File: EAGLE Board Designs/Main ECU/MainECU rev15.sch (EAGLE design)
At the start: 334 parts, among them J1 CONNECTOR-24_CONNECTOR-24_, J2 CONNECTOR-24_CONNECTOR-24_, K1 RELAY_DPDT_07DSMT, K2 RELAY_DPDT_07DSMT, K3 RELAY_DPDT_07DSMT, K4 RELAY_DPDT_07DSMT, K5 RELAY_DPDT_07DSMT, Q1 TRANSISTOR_N_MOS__DMG3406L-7, Q2 TRANSISTOR_P_MOS_SOT-23_DMP30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, Q3 TRANSISTOR_P_MOS_SOT-23_DMP30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, Q4 TRANSISTOR_N_MOS__DMG3406L-7, T1 TRANSFORMER_HM2112ZNLT, U1 VOLTAGE_REGULATOR_SOT-223_3.3V, U10 LOGICGATE_OR, U11 LOGICGATE_OR, U12 LOGICGATE_OR, U13 LOGICGATE_NOR, U14 TCAN1051HQV-Q1, U15 LOGICGATE_AND_DCK3, U16 MAX3074EESA+, U17 LTC1563, U18 LTC1563, U19 LTC1563, U2 LTC6820, U20 LTC1563, U21 LTC1563, U22 LTC1563, U23 LTC1563, U24 OPAMP_2_CHANNEL_OPA_2991, U25 OPAMP_2_CHANNEL_OPA_2991, U26 OPAMP_2_CHANNEL_OPA_2991, U27 OPAMP_2_CHANNEL_OPA_2991, U28 LTC1563, U29 TCAN1051HQV-Q1, U3 LTC6820, U30 TCAN1051HQV-Q1, U31 ADM8316WBX30, U4 TCAN1051HQV-Q1, U5 LTC1563, U6 MCP3208, U7 OPAMP_1_CHANNEL_OPA991, U8 LOGICGATE_OR, U9 LOGICGATE_OR

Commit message: going crazy
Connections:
- net BRAKELIGHT_EN: now also A2.D8; no longer A2.D7
- net INVERTER_24V_EN: now also A2.D7; no longer A2.D8

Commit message: DRC
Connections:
- removed net !STEERING_2_CS: A2.(CS)D10
- new net LPA10: R77.2, R81.2, U18.LPA
- net BRAKELIGHT_EN: now also A2.D6; no longer A2.D8
- net LPA: no longer R77.2, R81.2, U18.LPA
- net SHDN_C_READ: now also A2.(CS)D10; no longer A2.A17
- net SOFTWARE_OK: now also A2.D8; no longer A2.D28

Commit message: shifted stuff over
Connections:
- net BRAKE_1_EXT: now also J2.18; no longer J2.17
- net BRAKE_2_EXT: now also J2.17; no longer J2.18
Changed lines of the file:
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@@
-</segment>
-</net>
-<net name="BRAKE_1_EXT" class="0">
-<segment>
-<wire x1="111.76" y1="127" x2="119.38" y2="127" width="0.1524" layer="91"/>
-<label x="119.38" y="127" size="1.27" layer="95" xref="yes"/>
-<pinref part="J2" gate="G$1" pin="17"/>
 </segment>
 </net>
 <net name="BRAKE_2_EXT" class="0">
 <segment>
-<wire x1="111.76" y1="124.46" x2="119.38" y2="124.46" width="0.1524" layer="91"/>
-<label x="119.38" y="124.46" size="1.27" layer="95" xref="yes"/>
-<pinref part="J2" gate="G$1" pin="18"/>
+<wire x1="111.76" y1="127" x2="119.38" y2="127" width="0.1524" layer="91"/>
+<pinref part="J2" gate="G$1" pin="17"/>
+<label x="119.38" y="127" size="1.27" layer="95" xref="yes"/>
 </segment>
 </net>
@@
 </segment>
 </net>
+<net name="BRAKE_1_EXT" class="0">
+<segment>
+<wire x1="111.76" y1="124.46" x2="119.38" y2="124.46" width="0.1524" layer="91"/>
+<label x="119.38" y="124.46" size="1.27" layer="95" xref="yes"/>
+<pinref part="J2" gate="G$1" pin="18"/>
+</segment>
+</net>

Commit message: finito
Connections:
- new net LPA20: R73.2, R75.2, U17.LPA
- net LPA: no longer R73.2, R75.2, U17.LPA

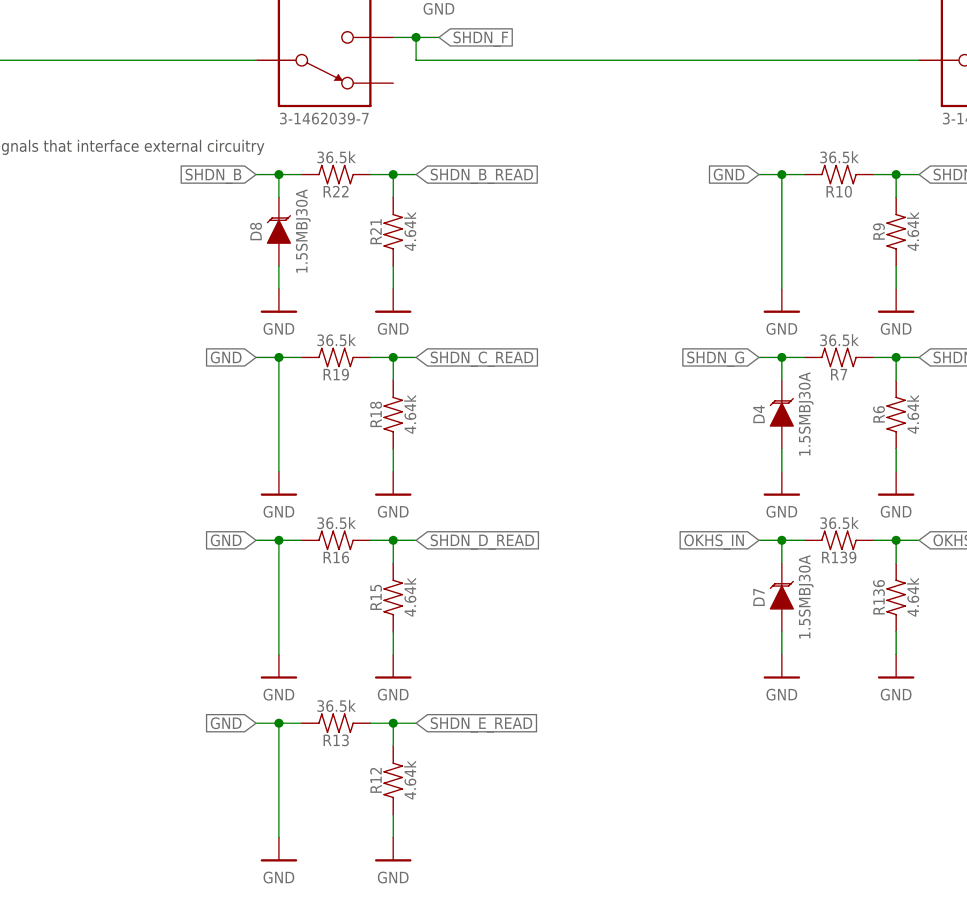
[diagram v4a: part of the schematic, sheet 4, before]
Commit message: mikhail prelim review
changes that need to be made have been recorded
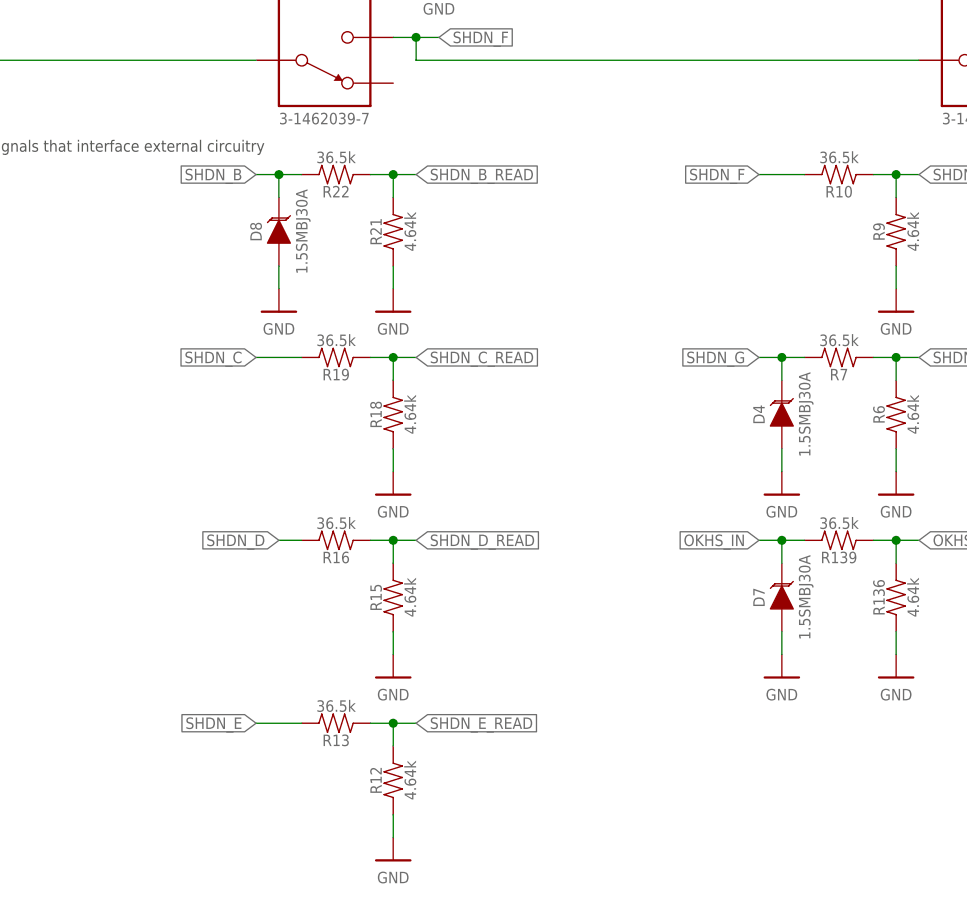
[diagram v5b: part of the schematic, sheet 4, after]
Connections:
- net GND: no longer R10.2, R13.2, R16.2, R19.2
- net SHDN_C: now also R19.2
- net SHDN_D: now also R16.2
- net SHDN_E: now also R13.2
- net SHDN_F: now also R10.2
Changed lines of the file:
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@@
 <part name="P289" library="HyTechSupplies" deviceset="GND" device=""/>
 <part name="R18" library="HyTechDevices" deviceset="RESISTOR_?_*" device="0603" technology="4.64K" value="RESISTOR_0603_4.64K"/>
-<part name="P290" library="HyTechSupplies" deviceset="GND" device=""/>
 <part name="R16" library="HyTechDevices" deviceset="RESISTOR_?_*" device="0603" technology="36.5K" value="RESISTOR_0603_36.5K"/>
 <part name="P291" library="HyTechSupplies" deviceset="GND" device=""/>
 <part name="R15" library="HyTechDevices" deviceset="RESISTOR_?_*" device="0603" technology="4.64K" value="RESISTOR_0603_4.64K"/>
-<part name="P292" library="HyTechSupplies" deviceset="GND" device=""/>
 <part name="R13" library="HyTechDevices" deviceset="RESISTOR_?_*" device="0603" technology="36.5K" value="RESISTOR_0603_36.5K"/>
 <part name="P293" library="HyTechSupplies" deviceset="GND" device=""/>
 <part name="R12" library="HyTechDevices" deviceset="RESISTOR_?_*" device="0603" technology="4.64K" value="RESISTOR_0603_4.64K"/>
-<part name="P294" library="HyTechSupplies" deviceset="GND" device=""/>
 <part name="R10" library="HyTechDevices" deviceset="RESISTOR_?_*" device="0603" technology="36.5K" value="RESISTOR_0603_36.5K"/>
 <part name="P295" library="HyTechSupplies" deviceset="GND" device=""/>
 <part name="R9" library="HyTechDevices" deviceset="RESISTOR_?_*" device="0603" technology="4.64K" value="RESISTOR_0603_4.64K"/>
-<part name="P296" library="HyTechSupplies" deviceset="GND" device=""/>
 <part name="R7" library="HyTechDevices" deviceset="RESISTOR_?_*" device="0603" technology="36.5K" value="RESISTOR_0603_36.5K"/>
 <part name="P297" library="HyTechSupplies" deviceset="GND" device=""/>
@@
 <attribute name="RESISTANCE" x="59.69" y="74.93" size="1.27" layer="96" rot="R90" align="top-center"/>
 </instance>
-<instance part="P290" gate="1" x="45.72" y="66.04" smashed="yes">
-<attribute name="VALUE" x="45.72" y="64.77" size="1.27" layer="96" align="top-center"/>
-</instance>
 <instance part="R16" gate="G$1" x="50.8" y="60.96" smashed="yes" rot="R180">
 <attribute name="NAME" x="52.07" y="59.69" size="1.27" layer="95" rot="R180" align="bottom-center"/>
@@
 <attribute name="RESISTANCE" x="59.69" y="54.61" size="1.27" layer="96" rot="R90" align="top-center"/>
 </instance>
-<instance part="P292" gate="1" x="45.72" y="45.72" smashed="yes">
-<attribute name="VALUE" x="45.72" y="44.45" size="1.27" layer="96" align="top-center"/>
-</instance>
 <instance part="R13" gate="G$1" x="50.8" y="40.64" smashed="yes" rot="R180">
 <attribute name="NAME" x="52.07" y="39.37" size="1.27" layer="95" rot="R180" align="bottom-center"/>
@@
 <attribute name="RESISTANCE" x="59.69" y="34.29" size="1.27" layer="96" rot="R90" align="top-center"/>
 </instance>
-<instance part="P294" gate="1" x="45.72" y="25.4" smashed="yes">
-<attribute name="VALUE" x="45.72" y="24.13" size="1.27" layer="96" align="top-center"/>
-</instance>
 <instance part="R10" gate="G$1" x="106.68" y="101.6" smashed="yes" rot="R180">
 <attribute name="NAME" x="107.95" y="100.33" size="1.27" layer="95" rot="R180" align="bottom-center"/>
@@
 <attribute name="RESISTANCE" x="115.57" y="95.25" size="1.27" layer="96" rot="R90" align="top-center"/>
 </instance>
-<instance part="P296" gate="1" x="101.6" y="86.36" smashed="yes">
-<attribute name="VALUE" x="101.6" y="85.09" size="1.27" layer="96" align="top-center"/>
-</instance>
 <instance part="R7" gate="G$1" x="106.68" y="81.28" smashed="yes" rot="R180">
 <attribute name="NAME" x="107.95" y="80.01" size="1.27" layer="95" rot="R180" align="bottom-center"/>
@@
 </segment>
 <segment>
-<pinref part="P290" gate="1" pin="GND"/>
-<label x="43.18" y="81.28" size="1.27" layer="95" rot="R180" xref="yes"/>
-<pinref part="R19" gate="G$1" pin="2"/>
-<wire x1="48.26" y1="81.28" x2="45.72" y2="81.28" width="0.1524" layer="91"/>
-<wire x1="45.72" y1="81.28" x2="43.18" y2="81.28" width="0.1524" layer="91"/>
-<junction x="45.72" y="81.28"/>
-<wire x1="45.72" y1="81.28" x2="45.72" y2="68.58" width="0.1524" layer="91"/>
-</segment>
-<segment>
 <pinref part="P291" gate="1" pin="GND"/>
 <pinref part="R15" gate="G$1" pin="1"/>
@@
 </segment>
 <segment>
-<pinref part="P292" gate="1" pin="GND"/>
-<label x="43.18" y="60.96" size="1.27" layer="95" rot="R180" xref="yes"/>
-<pinref part="R16" gate="G$1" pin="2"/>
-<wire x1="48.26" y1="60.96" x2="45.72" y2="60.96" width="0.1524" layer="91"/>
-<wire x1="45.72" y1="60.96" x2="43.18" y2="60.96" width="0.1524" layer="91"/>
-<junction x="45.72" y="60.96"/>
-<wire x1="45.72" y1="48.26" x2="45.72" y2="60.96" width="0.1524" layer="91"/>
-</segment>
-<segment>
 <pinref part="P293" gate="1" pin="GND"/>
 <pinref part="R12" gate="G$1" pin="1"/>
@@
 </segment>
 <segment>
-<pinref part="P294" gate="1" pin="GND"/>
-<label x="43.18" y="40.64" size="1.27" layer="95" rot="R180" xref="yes"/>
-<pinref part="R13" gate="G$1" pin="2"/>
-<wire x1="48.26" y1="40.64" x2="45.72" y2="40.64" width="0.1524" layer="91"/>
-<wire x1="45.72" y1="40.64" x2="43.18" y2="40.64" width="0.1524" layer="91"/>
-<junction x="45.72" y="40.64"/>
-<wire x1="45.72" y1="40.64" x2="45.72" y2="27.94" width="0.1524" layer="91"/>
-</segment>
-<segment>
 <pinref part="P295" gate="1" pin="GND"/>
 <pinref part="R9" gate="G$1" pin="1"/>
@@
 </segment>
 <segment>
-<pinref part="P296" gate="1" pin="GND"/>
-<label x="99.06" y="101.6" size="1.27" layer="95" rot="R180" xref="yes"/>
-<pinref part="R10" gate="G$1" pin="2"/>
-<wire x1="104.14" y1="101.6" x2="101.6" y2="101.6" width="0.1524" layer="91"/>
-<wire x1="101.6" y1="101.6" x2="99.06" y2="101.6" width="0.1524" layer="91"/>
-<junction x="101.6" y="101.6"/>
-<wire x1="101.6" y1="101.6" x2="101.6" y2="88.9" width="0.1524" layer="91"/>
-</segment>
-<segment>
 <pinref part="P297" gate="1" pin="GND"/>
 <pinref part="R6" gate="G$1" pin="1"/>
@@
 <junction x="60.96" y="172.72"/>
 </segment>
+<segment>
+<pinref part="R19" gate="G$1" pin="2"/>
+<wire x1="48.26" y1="81.28" x2="43.18" y2="81.28" width="0.1524" layer="91"/>
+<label x="43.18" y="81.28" size="1.27" layer="95" rot="R180" xref="yes"/>
+</segment>
 </net>
 <net name="SHDN_D" class="0">
@@
 <label x="137.16" y="172.72" size="1.27" layer="95" xref="yes"/>
 </segment>
+<segment>
+<pinref part="R16" gate="G$1" pin="2"/>
+<wire x1="48.26" y1="60.96" x2="45.72" y2="60.96" width="0.1524" layer="91"/>
+<label x="45.72" y="60.96" size="1.27" layer="95" rot="R180" xref="yes"/>
+</segment>
 </net>
 <net name="SHDN_E" class="0">
@@
 <wire x1="7.62" y1="114.3" x2="43.18" y2="114.3" width="0.1524" layer="91"/>
 </segment>
+<segment>
+<label x="43.18" y="40.64" size="1.27" layer="95" rot="R180" xref="yes"/>
+<pinref part="R13" gate="G$1" pin="2"/>
+<wire x1="48.26" y1="40.64" x2="43.18" y2="40.64" width="0.1524" layer="91"/>
+</segment>
 </net>
 <net name="SHDN_B_READ" class="0">
@@
 <junction x="60.96" y="116.84"/>
 </segment>
+<segment>
+<label x="99.06" y="101.6" size="1.27" layer="95" rot="R180" xref="yes"/>
+<pinref part="R10" gate="G$1" pin="2"/>
+<wire x1="104.14" y1="101.6" x2="99.06" y2="101.6" width="0.1524" layer="91"/>
+</segment>
 </net>

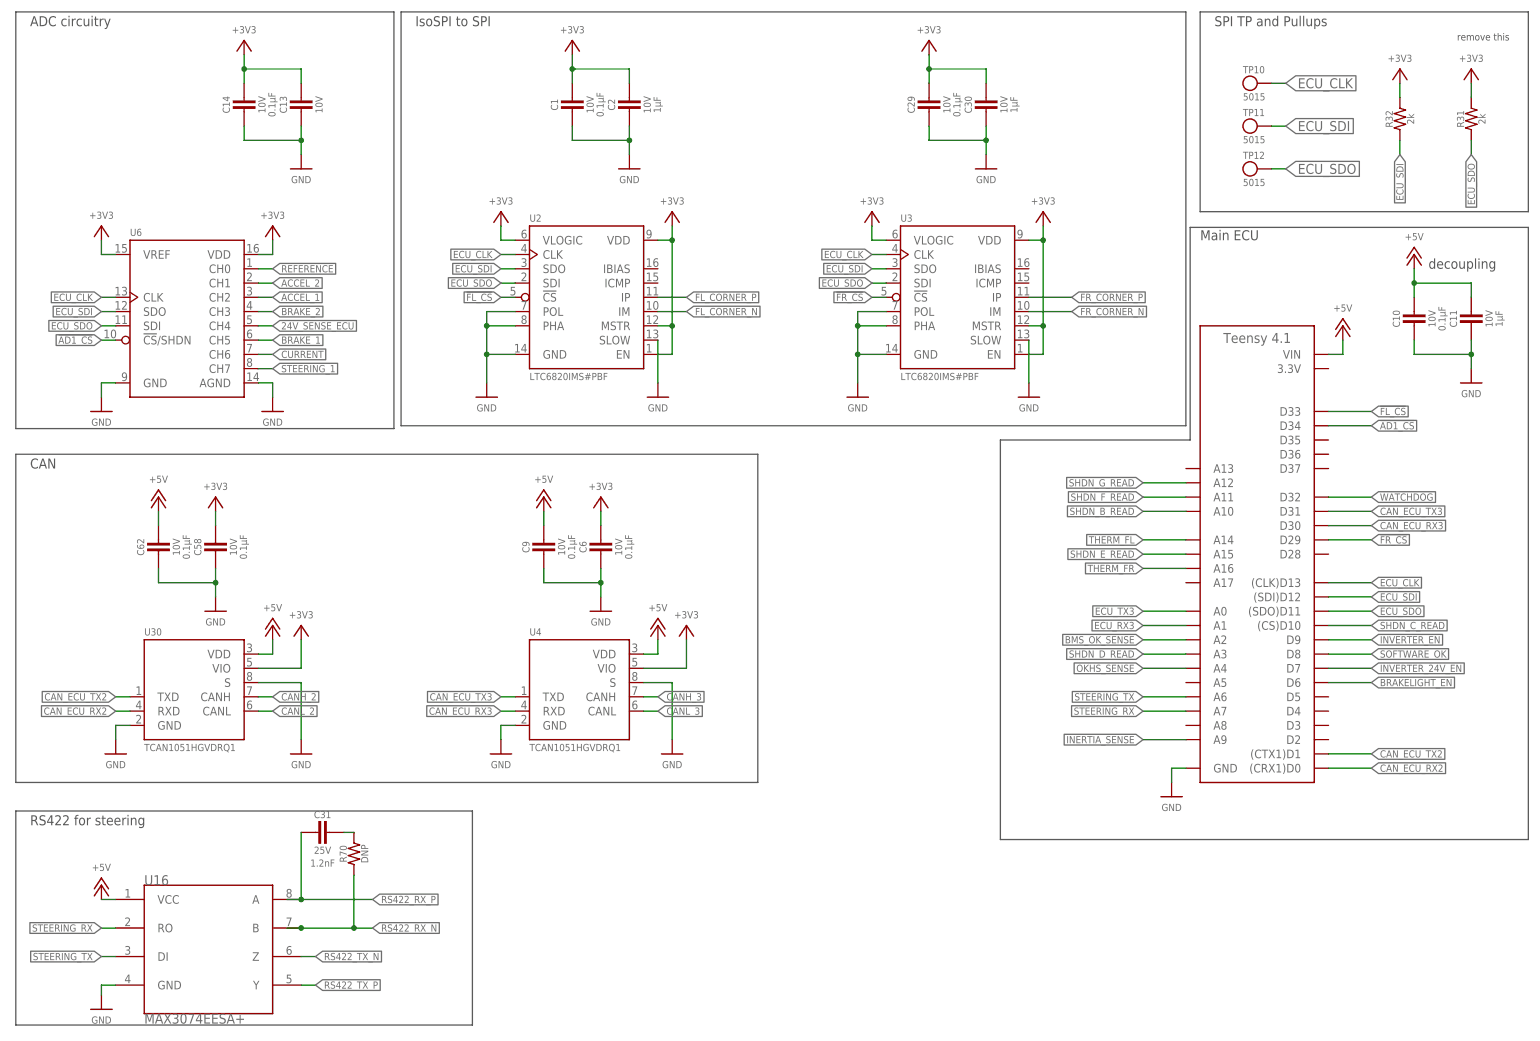
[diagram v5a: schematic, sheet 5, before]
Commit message: isospi needs to change
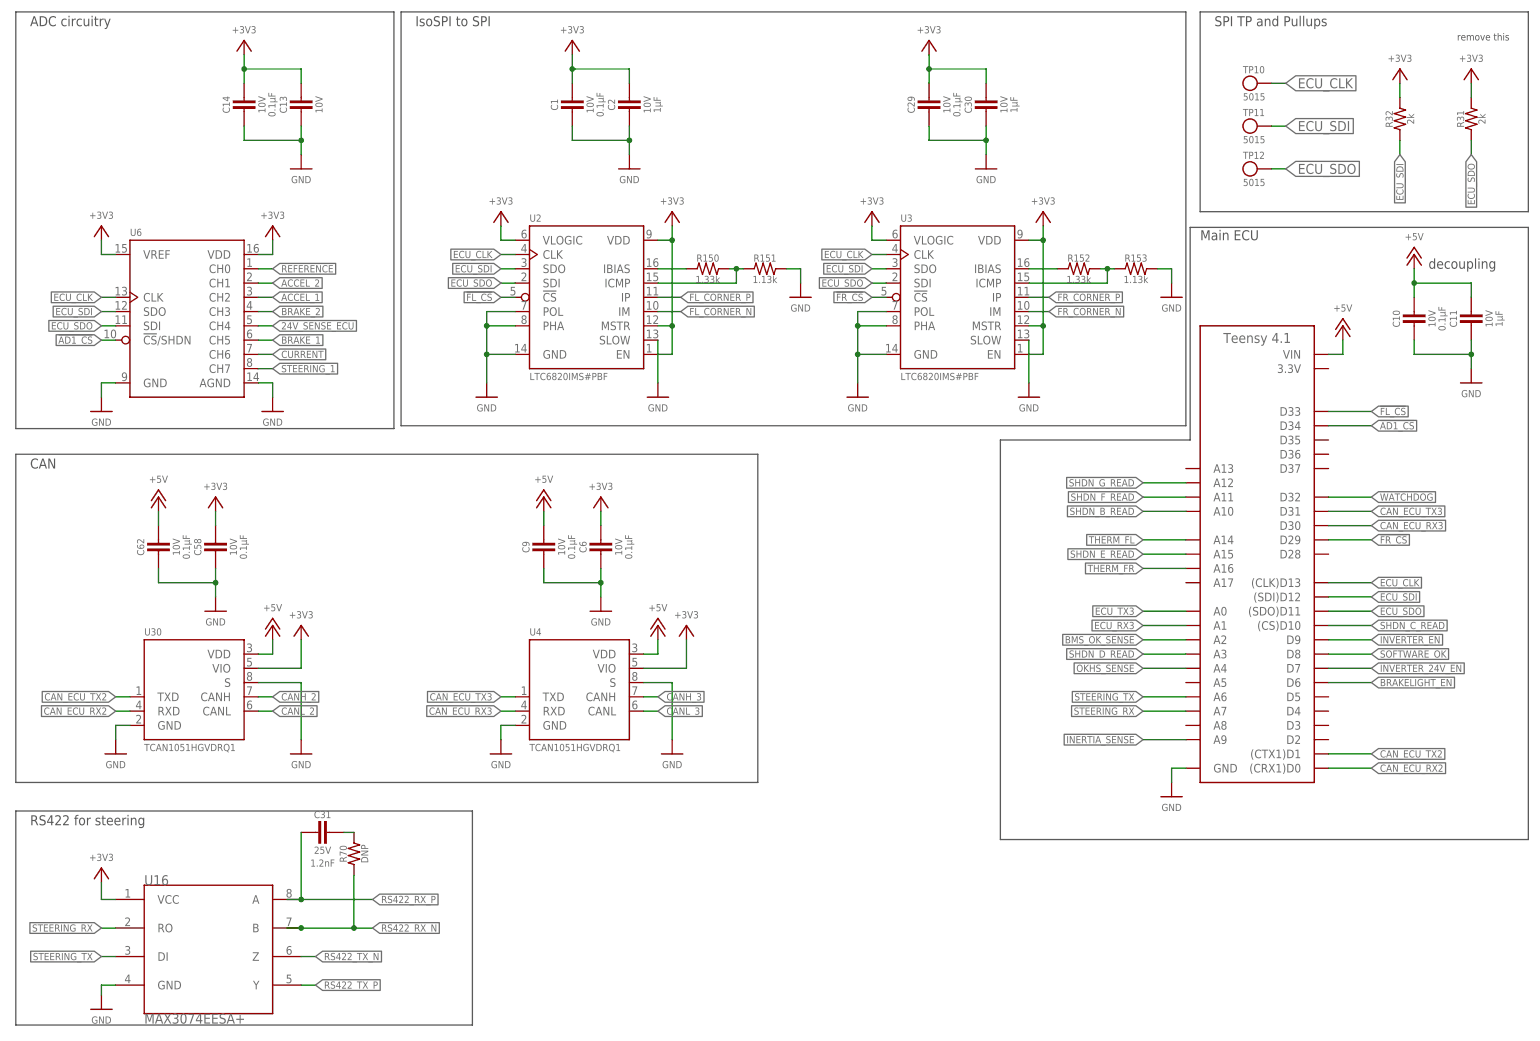
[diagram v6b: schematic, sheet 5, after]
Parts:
- added R150, R152: RESISTOR_0603_1.33K, HyTechDevices:RESISTOR_0603_1.33K
- added R151, R153: RESISTOR_0603_1.13K, HyTechDevices:RESISTOR_0603_1.13K
- R66: value RESISTOR_0603_2.18K -> RESISTOR_0603_2.55K; device HyTechDevices:RESISTOR_0603_2.18K -> HyTechDevices:RESISTOR_0603_2.55K
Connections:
- net 2V72 renamed 2V65
- removed net 0V59: R68.2, R69.2, U27B.VIN+
- new net N$10: R150.1, U2.IBIAS
- new net N$62: R150.2, R151.1, U2.ICMP
- new net N$66: R152.1, U3.IBIAS
- new net N$69: R152.2, R153.1, U3.ICMP
- net +3V3: now also U16.VCC
- net +5V: no longer U16.VCC
- net 0V26: now also R68.2, R69.2, U27B.VIN+
- net GND: now also R151.2, R153.2
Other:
- note added: "BRAKE_MISSING CALCULATIONS BRAKE_OOR_LO: 0.5 V * 0.6 = 0.30 .worst case input open circuit BRAKE_OOR_HI: 4.5V * .6 = 2.7 worst case input supply short circuit"
- note removed: "BRAKE_MISSING CALCULATIONS BRAKE_OOR_LO: 0.9 V * 0.6 = 0.54 Based off of lowest input voltage of 4.5 times voltage divider, rotated at -20 degrees from center. BRAKE_OOR_HI: 4.4V * .6 = 2.65 Based off of highest input voltage of 5.5, rotated at 25 degrees from center. (max travel of 20)"

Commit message: done day
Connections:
- new net 0V26_1: R68.2, R69.2, U27B.VIN+
- net 0V26: no longer R68.2, R69.2, U27B.VIN+
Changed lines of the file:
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@@
 <pinref part="U26" gate="B" pin="VIN+"/>
-</segment>
-<segment>
-<pinref part="R69" gate="G$1" pin="2"/>
-<pinref part="R68" gate="G$1" pin="2"/>
-<wire x1="210.82" y1="200.66" x2="213.36" y2="200.66" width="0.1524" layer="91"/>
-<wire x1="213.36" y1="200.66" x2="213.36" y2="198.12" width="0.1524" layer="91"/>
-<wire x1="213.36" y1="200.66" x2="215.9" y2="200.66" width="0.1524" layer="91"/>
-<junction x="213.36" y="200.66"/>
-<label x="215.9" y="200.66" size="1.27" layer="95" xref="yes"/>
-</segment>
-<segment>
-<wire x1="109.22" y1="152.4" x2="106.68" y2="152.4" width="0.1524" layer="91"/>
-<label x="106.68" y="152.4" size="1.27" layer="95" rot="R180" xref="yes"/>
-<pinref part="U27" gate="B" pin="VIN+"/>
 </segment>
 </net>
@@
 </segment>
 </net>
+<net name="0V26_1" class="0">
+<segment>
+<pinref part="R69" gate="G$1" pin="2"/>
+<pinref part="R68" gate="G$1" pin="2"/>
+<wire x1="210.82" y1="200.66" x2="213.36" y2="200.66" width="0.1524" layer="91"/>
+<wire x1="213.36" y1="200.66" x2="213.36" y2="198.12" width="0.1524" layer="91"/>
+<wire x1="213.36" y1="200.66" x2="215.9" y2="200.66" width="0.1524" layer="91"/>
+<junction x="213.36" y="200.66"/>
+<label x="215.9" y="200.66" size="1.27" layer="95" xref="yes"/>
+</segment>
+<segment>
+<wire x1="109.22" y1="152.4" x2="106.68" y2="152.4" width="0.1524" layer="91"/>
+<label x="106.68" y="152.4" size="1.27" layer="95" rot="R180" xref="yes"/>
+<pinref part="U27" gate="B" pin="VIN+"/>
+</segment>
+</net>
